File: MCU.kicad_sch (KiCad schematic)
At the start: 0 parts

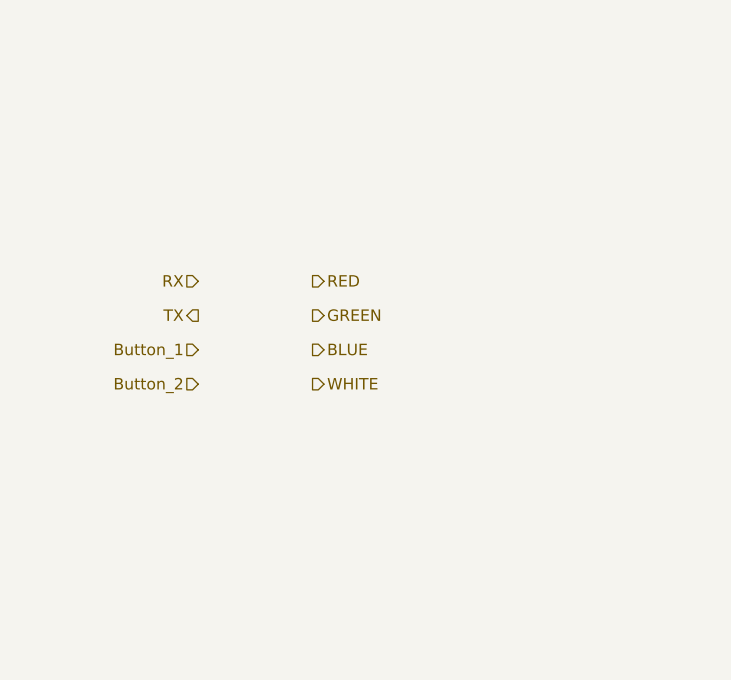
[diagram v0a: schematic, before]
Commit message: added usb serial and mcu
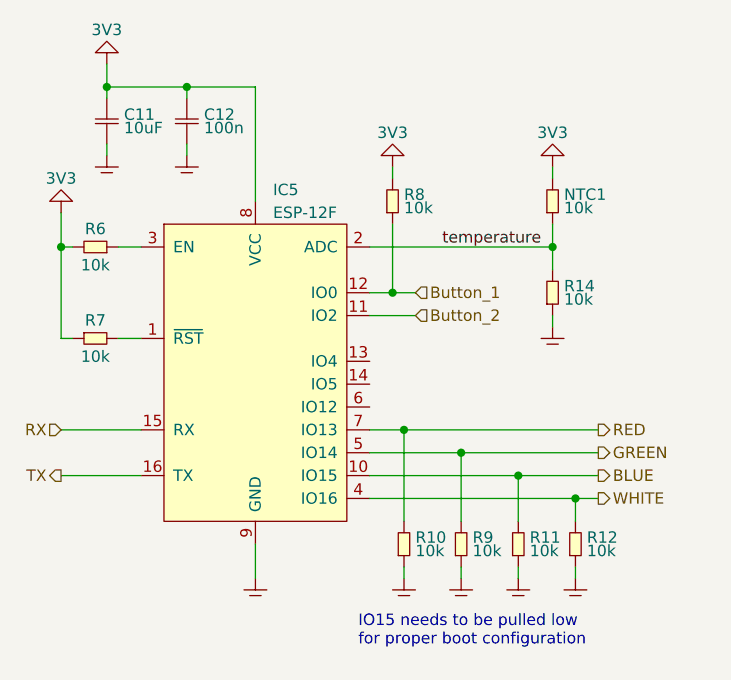
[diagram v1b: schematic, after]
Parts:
- added C11: 10uF, SMT:0603, symbol generic:C
- added C12: 100n, SMT:0603, symbol generic:C
- added IC5: ESP-12F, symbol modules:ESP-12F
- added NTC1, R10, R11, R12, R14, R6, R7, R8, R9: 10k, SMT:0603, symbol generic:R
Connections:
- net BLUE: now also IC5.10 (IO15), R11.2
- net Button_1: now also IC5.12 (IO0), R8.1
- net Button_2: now also IC5.11 (IO2)
- net GREEN: now also IC5.5 (IO14), R9.2
- net RED: now also IC5.7 (IO13), R10.2
- net RX: now also IC5.15 (RX)
- net TX: now also IC5.16 (TX)
- net WHITE: now also IC5.4 (IO16), R12.2
- new net: IC5.3 (EN), R6.1
- new net: IC5.1 (~{RST}), R7.2
- new net GND: C11.1, C11.2, C12.1, C12.2, IC5.8 (VCC), IC5.9 (GND), NTC1.2, R10.1, R11.1, R12.1, R14.1, R6.2, R7.1, R8.2, R9.1
- new net temperature: IC5.2 (ADC), NTC1.1, R14.2
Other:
- note added: "IO15 needs to be pulled low for proper boot configuration"

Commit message: cleaned up layout, added 3V3 regulator, changed NTC to connect to gnd instead of 3V3, added README
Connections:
- net GND: now also NTC1.1, R14.2; no longer NTC1.2, R14.1
- net temperature: now also NTC1.2, R14.1; no longer NTC1.1, R14.2
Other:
- moved on the sheet: C11, C12, IC5, NTC1, R10, R11, R12, R14, R6, R7, R8, R9

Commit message: added esp12 footprint
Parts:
- IC5: footprint (none) -> espressif:ESP-12F
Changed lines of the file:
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@@
       (effects (font (size 1.27 1.27)) (justify left))
     )
-    (property "Footprint" "" (at 134.62 101.6 0)
+    (property "Footprint" "espressif:ESP-12F" (at 134.62 101.6 0)
       (effects (font (size 1.27 1.27)) hide)
     )

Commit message: worked layout, fixed 3V3 being GND net
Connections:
- net GND: no longer C11.1, C12.1, IC5.8 (VCC), R14.2, R6.2, R7.1, R8.2
- new net 3V3: C11.1, C12.1, IC5.8 (VCC), R14.2, R6.2, R7.1, R8.2

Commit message: did most of todo items
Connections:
- net BLUE: now also IC5.6 (IO12), R10.2; no longer IC5.10 (IO15), R11.2
- net GREEN: now also R11.2; no longer R9.2
- net RED: now also IC5.4 (IO16), R12.2; no longer IC5.7 (IO13), R10.2
- net WHITE: now also IC5.7 (IO13), R9.2; no longer IC5.4 (IO16), R12.2
- net Button_2 renamed LED_strip
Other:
- moved on the sheet: R10, R11, R12

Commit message: added Digi-Key part numbers to BOM
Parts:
- C11: Digi-Key (none) -> 1276-1119-1-ND
- C12: Digi-Key (none) -> 1276-1935-1-ND
- NTC1: Digi-Key (none) -> 490-16279-1-ND
- R10, R11, R12, R14, R6, R7, R8, R9: Digi-Key (none) -> 13-RC0603JR-1010KLCT-ND
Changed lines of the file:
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@@
+      (effects (font (size 1.27 1.27)) hide)
+    )
+    (property "Digi-Key" "13-RC0603JR-1010KLCT-ND" (at 167.64 81.28 0)
       (effects (font (size 1.27 1.27)) hide)
     )
@@
     )
     (property "Datasheet" "" (at 157.48 119.38 0)
+      (effects (font (size 1.27 1.27)) hide)
+    )
+    (property "Digi-Key" "13-RC0603JR-1010KLCT-ND" (at 157.48 119.38 0)
       (effects (font (size 1.27 1.27)) hide)
     )
@@
       (effects (font (size 1.27 1.27)) hide)
     )
+    (property "Digi-Key" "1276-1935-1-ND" (at 127 72.39 0)
+      (effects (font (size 1.27 1.27)) hide)
+    )
     (pin "1")
     (pin "2")
@@
     )
     (property "Datasheet" "" (at 167.64 91.44 0)
+      (effects (font (size 1.27 1.27)) hide)
+    )
+    (property "Digi-Key" "490-16279-1-ND" (at 167.64 91.44 0)
       (effects (font (size 1.27 1.27)) hide)
     )
@@
     )
     (property "Datasheet" "" (at 118.11 72.39 0)
+      (effects (font (size 1.27 1.27)) hide)
+    )
+    (property "Digi-Key" "1276-1119-1-ND" (at 118.11 72.39 0)
       (effects (font (size 1.27 1.27)) hide)
     )
@@
       (effects (font (size 1.27 1.27)) hide)
     )
+    (property "Digi-Key" "13-RC0603JR-1010KLCT-ND" (at 172.72 119.38 0)
+      (effects (font (size 1.27 1.27)) hide)
+    )
     (pin "1")
     (pin "2")
@@
       (effects (font (size 1.27 1.27)) hide)
     )
+    (property "Digi-Key" "13-RC0603JR-1010KLCT-ND" (at 165.1 119.38 0)
+      (effects (font (size 1.27 1.27)) hide)
+    )
     (pin "1")
     (pin "2")
@@
     )
     (property "Datasheet" "" (at 149.86 119.38 0)
+      (effects (font (size 1.27 1.27)) hide)
+    )
+    (property "Digi-Key" "13-RC0603JR-1010KLCT-ND" (at 149.86 119.38 0)
       (effects (font (size 1.27 1.27)) hide)
     )
@@
     )
     (property "Datasheet" "" (at 116.84 86.36 0)
+      (effects (font (size 1.27 1.27)) hide)
+    )
+    (property "Digi-Key" "13-RC0603JR-1010KLCT-ND" (at 116.84 86.36 0)
       (effects (font (size 1.27 1.27)) hide)
     )
@@
       (effects (font (size 1.27 1.27)) hide)
     )
+    (property "Digi-Key" "13-RC0603JR-1010KLCT-ND" (at 149.86 81.28 0)
+      (effects (font (size 1.27 1.27)) hide)
+    )
     (pin "1")
     (pin "2")
@@
       (effects (font (size 1.27 1.27)) hide)
     )
+    (property "Digi-Key" "13-RC0603JR-1010KLCT-ND" (at 116.84 96.52 0)
+      (effects (font (size 1.27 1.27)) hide)
+    )
